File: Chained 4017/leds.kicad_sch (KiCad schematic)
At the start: 50 parts

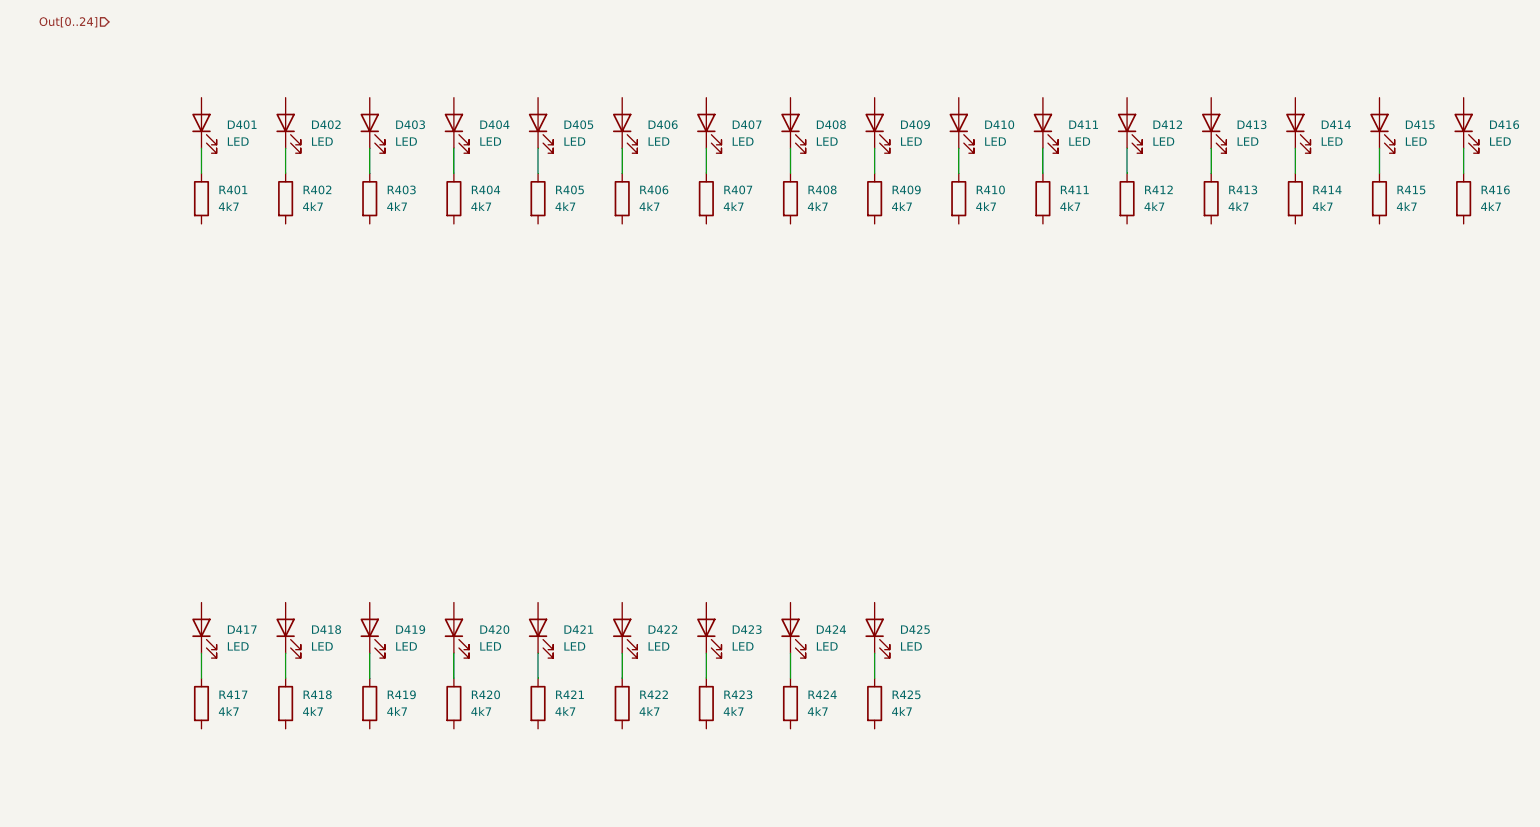
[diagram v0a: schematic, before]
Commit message: Layout and starting routing
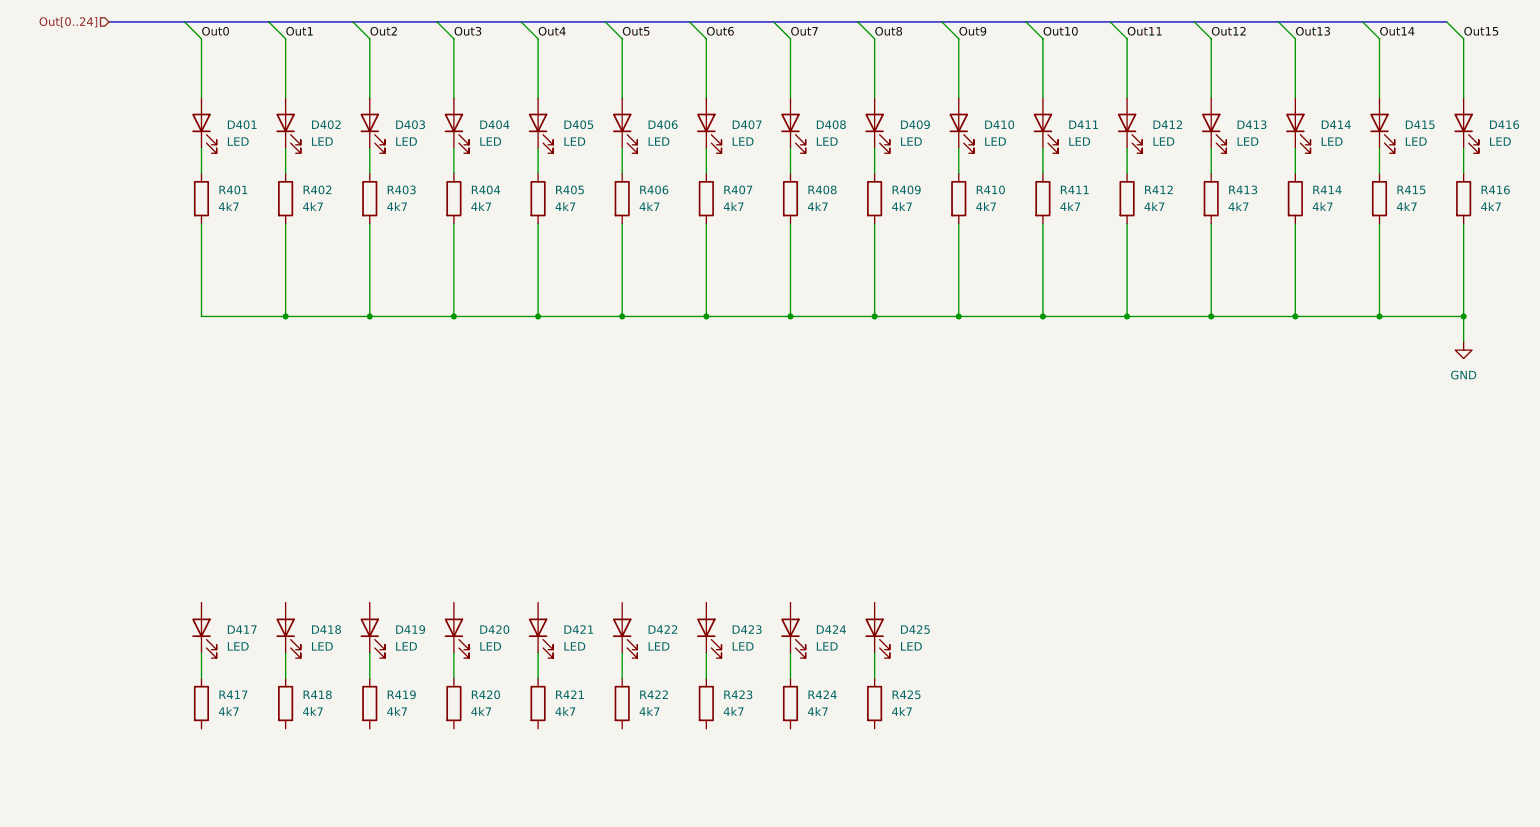
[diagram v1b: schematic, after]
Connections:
- net GND: now reaches R403.2
- net GND: now also R401.2, R402.2, R404.2, R405.2, R406.2, R407.2, R408.2, R409.2, R410.2, R411.2, R412.2, R413.2, R414.2, R415.2, R416.2
- net Out12: now reaches D413.2 (A)
- net Out10: now reaches D411.2 (A)
- net Out5: now reaches D406.2 (A)
- net Out0: now reaches D401.2 (A)
- net Out2: now reaches D403.2 (A)
- net Out4: now reaches D405.2 (A)
- net Out7: now reaches D408.2 (A)
- net Out13: now reaches D414.2 (A)
- net Out8: now reaches D409.2 (A)
- net Out11: now reaches D412.2 (A)
- net Out6: now reaches D407.2 (A)
- net Out1: now reaches D402.2 (A)
- net Out9: now reaches D410.2 (A)
- net Out3: now reaches D404.2 (A)
- net Out14: now reaches D415.2 (A)
- net Out15: now reaches D416.2 (A)

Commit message: Capacitors and routing
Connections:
- net GND: now also R417.2, R418.2, R419.2, R420.2, R421.2, R422.2, R423.2, R424.2, R425.2
- net Out18: now reaches D419.2 (A)
- net Out19: now reaches D420.2 (A)
- net Out20: now reaches D421.2 (A)
- net Out23: now reaches D424.2 (A)
- net Out17: now reaches D418.2 (A)
- net Out22: now reaches D423.2 (A)
- net Out21: now reaches D422.2 (A)
- net Out16: now reaches D417.2 (A)
- net Out24: now reaches D425.2 (A)
